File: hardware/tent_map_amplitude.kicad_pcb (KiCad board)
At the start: 4 copper layers, 58 x 61.8 mm, 57 parts, among them U1 LM339AN, U2 TL082IP, U3 TL082IP, U4 LF398_DIP8, U5 LF398_DIP8, U6 LF398_DIP8

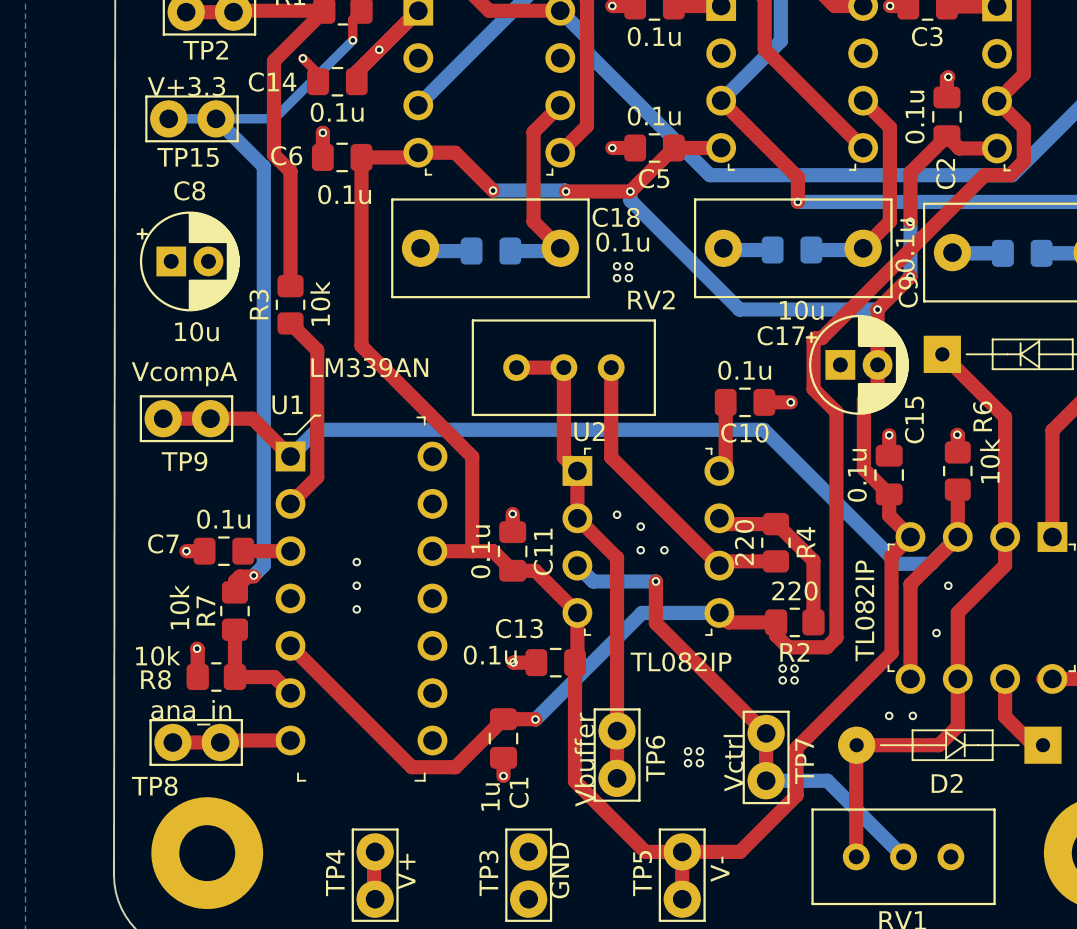
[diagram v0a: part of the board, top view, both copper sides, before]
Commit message: Use extra comparator for sampled bitstream output
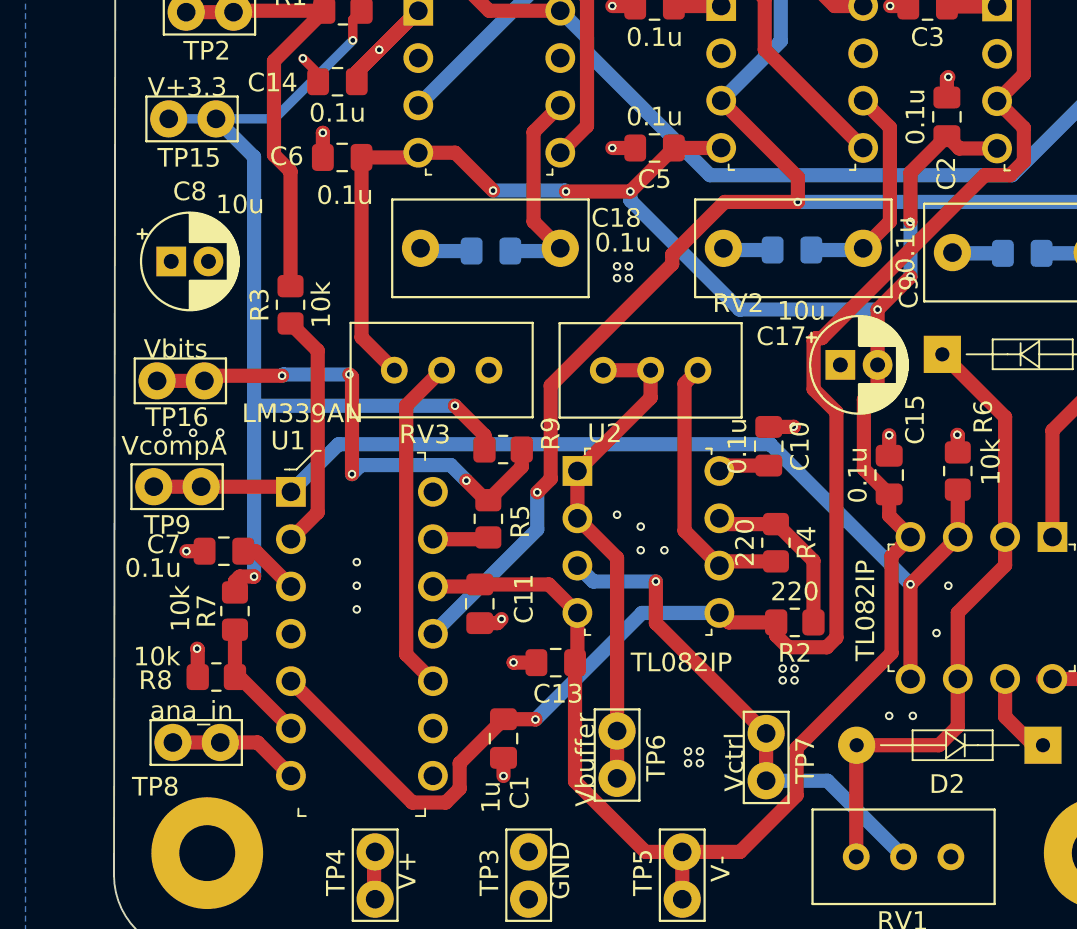
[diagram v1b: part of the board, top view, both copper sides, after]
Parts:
- added G***: LOGO, art:squad, B.Cu at (89.2, 102.3)
- added G***: LOGO, art:sawtooth, B.Cu at (76.3, 72.1)
- added R5: 10k, Resistor_SMD:R_0805_2012Metric_Pad1.20x1.40mm_HandSolder, F.Cu at (85.8, 91.0)
- added R9: 10k, Resistor_SMD:R_0805_2012Metric_Pad1.20x1.40mm_HandSolder, F.Cu at (86.6, 87.3)
- added RV3: R_POT, Potentiometer_THT:Potentiometer_Bourns_3296W_Vertical, F.Cu at (80.8, 83.0)
- added TP16: Vbits, TestPoint:TestPoint_Bridge_Pitch2.54mm_Drill1.0mm, F.Cu at (68.0, 83.6)
- moved RV2 4.66 mm to (97.1, 83.1)
- moved TP9 3.68 mm to (67.8, 89.3)
- moved C11 3.32 mm to (85.3, 95.6), turned to 90 degrees
- moved C10 2.68 mm to (100.9, 87.1), turned to 270 degrees
- moved U1 1.89 mm to (75.2, 89.6)
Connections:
- U1 pad 10: GND -> Net-(RV3-Pad2)
- U1 pad 11: V+ -> Net-(TP11-Pad1)
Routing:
- net Net-(TP11-Pad1): track 43.0 -> 76.6 mm, vias 1 -> 2
- net Net-(R5-Pad2): track 0.00 -> 27.6 mm, vias 0 -> 4
- net Net-(RV3-Pad2): track 0.00 -> 18.1 mm
- net V-: track 140.3 -> 128.1 mm
- net +3V3: track 42.3 -> 54.4 mm, vias 2 -> 3
- net Net-(R5-Pad1): track 0.00 -> 3.01 mm
- net Net-(R6-Pad2): track 58.9 -> 56.1 mm, vias 0 -> 1
- net Net-(R3-Pad1): track 10.9 -> 12.8 mm
- net Net-(C1-Pad1): track 87.4 -> 89.0 mm
- net Net-(R4-Pad2): track 16.2 -> 14.7 mm
- net Net-(RV2-Pad2): track 25.8 -> 27.0 mm
- net Net-(R7-Pad2): track 5.88 -> 6.69 mm
- net Net-(TP8-Pad1): track 6.36 -> 7.08 mm
- net GND: track 25.5 -> 25.7 mm, vias 53 -> 56
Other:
- board text added: "Chaotic Crew UAH Senior Design 2020 Tent Map CRNG"
- board text removed: "Chaotic Crew senior design 2020 tent map CRNG"

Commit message: Update PCB with previous commit changes
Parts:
- moved R3 14.8 mm to (74.0, 64.7)
- moved TP2 1.07 mm to (68.5, 63.7)
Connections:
- R3 pad 1: Net-(R3-Pad1) -> Net-(R1-Pad2)
- R3 pad 2: Net-(R1-Pad2) -> Net-(R3-Pad2)
- R9 pad 2: Net-(R5-Pad2) -> Net-(R5-Pad1)
- TP2 pad 1: Net-(R1-Pad2) -> Net-(R3-Pad2)
- U1 pad 2: Net-(R3-Pad1) -> Net-(R1-Pad2)
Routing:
- net Net-(R3-Pad1): track 12.8 -> 0.00 mm
- net Net-(R1-Pad2): track 23.7 -> 31.9 mm
- net Net-(R5-Pad1): track 3.01 -> 8.88 mm
- net Net-(R3-Pad2): track 0.00 -> 5.49 mm
- net Net-(R5-Pad2): track 27.6 -> 24.2 mm

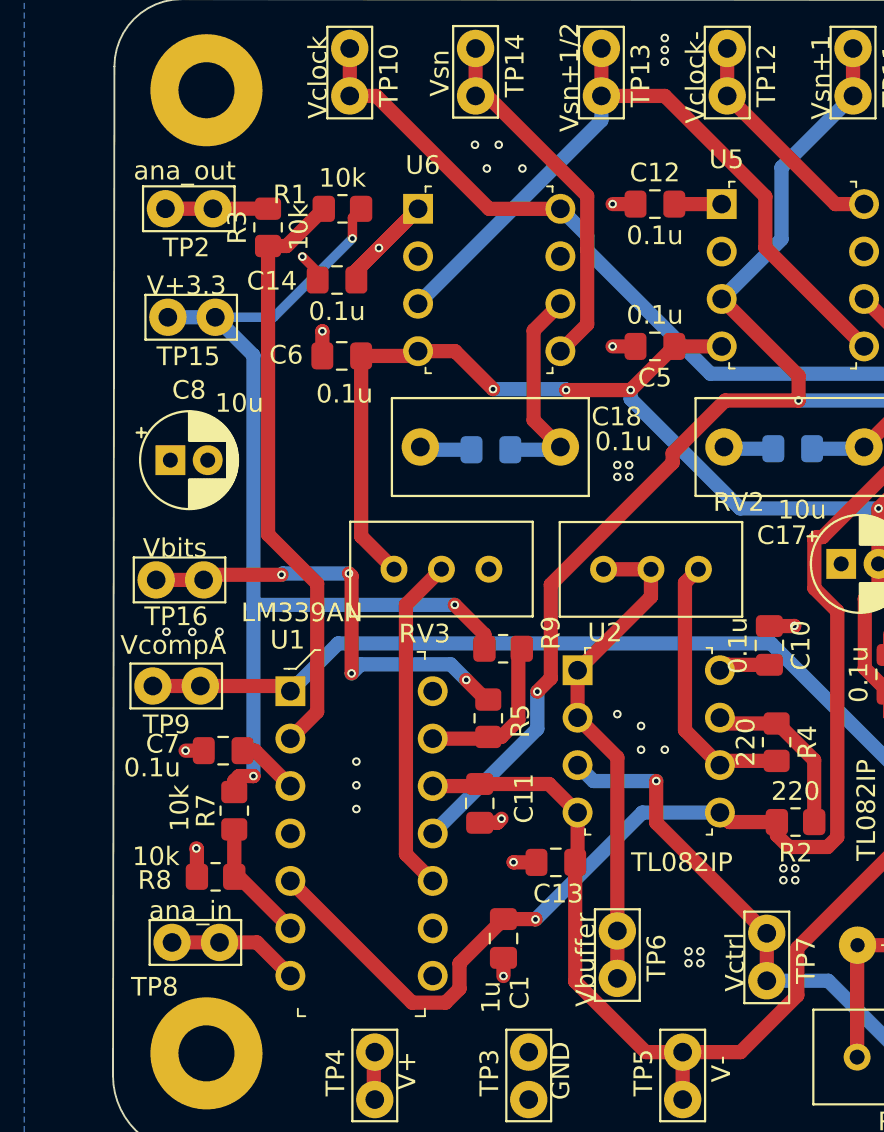
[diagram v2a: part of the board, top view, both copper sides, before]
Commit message: Change resistors back, change resistors to properly do 0v to 3.3v output, add power switch jumper, change references to 3.3v to Va+
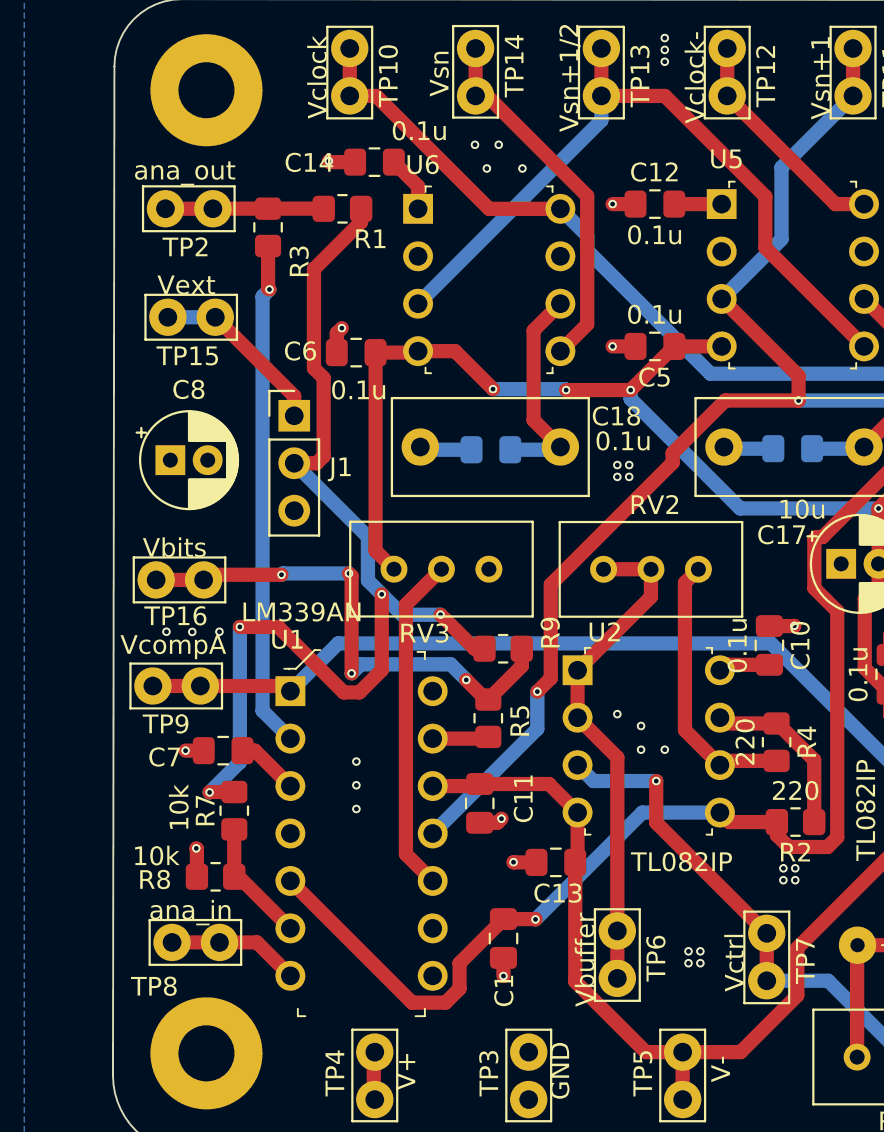
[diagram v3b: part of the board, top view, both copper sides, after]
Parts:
- added J1: Conn_01x03_Male, Connector_PinHeader_2.54mm:PinHeader_1x03_P2.54mm_Vertical, F.Cu at (75.4, 74.8)
- R1, R9: value 10k -> 6.65k
- TP15: value V+3.3 -> Vext
- moved C14 6.62 mm to (79.7, 61.3)
- moved C6 0.79 mm to (78.7, 71.5)
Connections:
- R1 pad 1: +3V3 -> Va+
- R3 pad 1: Net-(R1-Pad2) -> Net-(R3-Pad1)
- R3 pad 2: Net-(R3-Pad2) -> Net-(R1-Pad2)
- R7 pad 1: +3V3 -> Va+
- R9 pad 1: +3V3 -> Va+
- R9 pad 2: Net-(R5-Pad1) -> Net-(R5-Pad2)
- TP15 pad 1: +3V3 -> Net-(J1-Pad1)
- TP2 pad 1: Net-(R3-Pad2) -> Net-(R1-Pad2)
- U1 pad 14: Net-(U1-Pad14) -> (no net)
- U1 pad 2: Net-(R1-Pad2) -> Net-(R3-Pad1)
- U4 pad 2: Net-(U4-Pad2) -> (no net)
- U5 pad 2: Net-(U5-Pad2) -> (no net)
- U6 pad 2: Net-(U6-Pad2) -> (no net)
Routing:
- net Va+: track 0.00 -> 56.4 mm, vias 0 -> 4
- net +3V3: track 54.4 -> 0.00 mm, vias 3 -> 0
- net Net-(R3-Pad1): track 0.00 -> 27.2 mm, vias 0 -> 1
- net Net-(R1-Pad2): track 31.9 -> 8.48 mm
- net Net-(J1-Pad1): track 0.00 -> 12.1 mm
- net V+: track 29.2 -> 22.4 mm, vias 2 -> 1
- net Net-(R5-Pad1): track 8.88 -> 3.01 mm
- net Net-(R3-Pad2): track 5.49 -> 0.00 mm
- net Net-(R5-Pad2): track 24.2 -> 27.6 mm
- net V-: track 128.1 -> 127.1 mm

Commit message: Export gerbers gerbers for pcb V4
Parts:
- moved C8 51.6 mm to (119.2, 88.2)
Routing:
- net GND: vias 56 -> 48
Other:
- board text added: "V+"
- board text added: "Va+ select"
- board text added: "Vext"
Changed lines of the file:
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@@
   (general
     (thickness 1.6002)
-    (drawings 10)
-    (tracks 361)
+    (drawings 27)
+    (tracks 353)
     (zones 0)
     (modules 64)
@@
     (2 In2.Cu power)
     (31 Back signal)
-    (36 B.SilkS user hide)
+    (36 B.SilkS user)
     (37 F.SilkS user)
     (38 B.Mask user)
@@
     (45 Margin user)
     (46 B.CrtYd user)
-    (47 F.CrtYd user)
+    (47 F.CrtYd user hide)
     (49 F.Fab user hide)
   )
@@
       (effects (font (size 0.5 0.5) (thickness 0.08)))
     )
-    (pad 2 smd roundrect (at 1 0) (size 1.2 1.4) (layers Front F.Paste F.Mask) (roundrect_rratio 0.208333)
+    (pad 2 smd roundrect (at 1 0) (size 1.2 1.4) (layers Front F.Paste F.Mask) (roundrect_rratio 0.2083325)
       (net 25 "Net-(R5-Pad2)"))
-    (pad 1 smd roundrect (at -1 0) (size 1.2 1.4) (layers Front F.Paste F.Mask) (roundrect_rratio 0.208333)
+    (pad 1 smd roundrect (at -1 0) (size 1.2 1.4) (layers Front F.Paste F.Mask) (roundrect_rratio 0.2083325)
       (net 28 Va+))
     (model ${KISYS3DMOD}/Resistor_SMD.3dshapes/R_0805_2012Metric.wrl
@@
       (effects (font (size 0.5 0.5) (thickness 0.08)))
     )
-    (pad 2 smd roundrect (at 1 0 90) (size 1.2 1.4) (layers Front F.Paste F.Mask) (roundrect_rratio 0.208333)
+    (pad 2 smd roundrect (at 1 0 90) (size 1.2 1.4) (layers Front F.Paste F.Mask) (roundrect_rratio 0.2083325)
       (net 25 "Net-(R5-Pad2)"))
-    (pad 1 smd roundrect (at -1 0 90) (size 1.2 1.4) (layers Front F.Paste F.Mask) (roundrect_rratio 0.208333)
+    (pad 1 smd roundrect (at -1 0 90) (size 1.2 1.4) (layers Front F.Paste F.Mask) (roundrect_rratio 0.2083325)
       (net 26 "Net-(R5-Pad1)"))
     (model ${KISYS3DMOD}/Resistor_SMD.3dshapes/R_0805_2012Metric.wrl
@@
   )
   (module Capacitor_THT:CP_Radial_D5.0mm_P2.00mm (layer Front)
-    (at 68.78066 77.20838)
+    (at 119.21744 88.18372)
     (descr "CP, Radial series, Radial, pin pitch=2.00mm, , diameter=5mm, Electrolytic Capacitor")
     (tags "CP Radial series Radial pin pitch 2.00mm  diameter 5mm Electrolytic Capacitor")
-    (fp_text reference C8 (at 1 -3.75) (layer F.SilkS)
+    (fp_text reference C8 (at -1.5494 -3.0226) (layer F.SilkS)
       (effects (font (size 1 1) (thickness 0.15)))
     )
@@
   (module digikey-footprints:Diode_DO-35_P10mm (layer Front)
     (at 110.1674 82.1944)
-    (fp_text reference D1 (at 9.7536 2.6416) (layer F.SilkS)
+    (fp_text reference D1 (at 8.93828 -1.94056) (layer F.SilkS)
       (effects (font (size 1 1) (thickness 0.15)))
     )
@@
     )
   )
+  (gr_text "Va+ select" (at 69.54012 77.11948) (layer F.SilkS)
+    (effects (font (size 0.762 0.762) (thickness 0.127)))
+  )
+  (gr_line (start 72.88784 81.026) (end 73.69556 81.026) (layer F.SilkS) (width 0.127))
+  (gr_line (start 72.88784 77.70368) (end 72.88784 81.026) (layer F.SilkS) (width 0.127))
+  (gr_line (start 73.77176 77.70368) (end 72.88784 77.70368) (layer F.SilkS) (width 0.127))
+  (gr_line (start 72.51192 79.15656) (end 72.19696 79.44612) (layer F.SilkS) (width 0.127))
+  (gr_line (start 72.50176 79.10576) (end 72.25792 78.78572) (layer F.SilkS) (width 0.127))
+  (gr_line (start 71.3994 79.04988) (end 72.50176 79.10576) (layer F.SilkS) (width 0.127))
+  (gr_line (start 72.88276 77.37348) (end 73.74128 77.37348) (layer F.SilkS) (width 0.127))
+  (gr_line (start 72.88276 74.03592) (end 72.88276 77.37348) (layer F.SilkS) (width 0.127))
+  (gr_line (start 73.8124 74.03592) (end 72.88276 74.03592) (layer F.SilkS) (width 0.127))
+  (gr_line (start 72.75576 75.184) (end 72.37476 75.54468) (layer F.SilkS) (width 0.127))
+  (gr_line (start 72.75576 75.16368) (end 72.38492 74.86396) (layer F.SilkS) (width 0.127))
+  (gr_line (start 71.47052 75.1332) (end 72.75576 75.16368) (layer F.SilkS) (width 0.127))
+  (gr_line (start 71.6534 75.15352) (end 73.70064 75.09764) (layer Cmts.User) (width 0.15))
+  (gr_line (start 71.72452 75.08748) (end 73.8378 75.14336) (layer Cmts.User) (width 0.15))
+  (gr_text V+ (at 70.13448 79.07528) (layer F.SilkS)
+    (effects (font (size 1 1) (thickness 0.125) italic))
+  )
+  (gr_text Vext (at 69.6468 75.1078) (layer F.SilkS)
+    (effects (font (size 1 1) (thickness 0.15) italic))
+  )
   (gr_arc (start 120.141638 56.134) (end 123.698 56.134) (angle -90) (layer Edge.Cuts) (width 0.001))
   (gr_arc (start 69.3928 56.134) (end 69.3928 52.5272) (angle -90) (layer Edge.Cuts) (width 0.1))
@@
   (segment (start 110.4138 67.3862) (end 110.49 67.31) (width 0.762) (layer Front) (net 1))
   (segment (start 110.4138 68.41) (end 110.4138 67.3862) (width 0.762) (layer Front) (net 1) (status 10))
-  (via (at 96.52 103.505) (size 0.4572) (drill 0.254) (layers Front Back) (net 1))
-  (via (at 96.52 104.14) (size 0.4572) (drill 0.254) (layers Front Back) (net 1))
-  (via (at 97.155 104.14) (size 0.4572) (drill 0.254) (layers Front Back) (net 1))
-  (via (at 97.155 103.505) (size 0.4572) (drill 0.254) (layers Front Back) (net 1))
-  (via (at 101.6 99.06) (size 0.4572) (drill 0.254) (layers Front Back) (net 1))
-  (via (at 102.235 99.06) (size 0.4572) (drill 0.254) (layers Front Back) (net 1))
-  (via (at 102.235 99.695) (size 0.4572) (drill 0.254) (layers Front Back) (net 1))
-  (via (at 101.6 99.695) (size 0.4572) (drill 0.254) (layers Front Back) (net 1))
   (via (at 92.71 77.47) (size 0.4572) (drill 0.254) (layers Front Back) (net 1))
   (via (at 93.345 77.47) (size 0.4572) (drill 0.254) (layers Front Back) (net 1))
@@
   (via (at 108.585 101.6) (size 0.4572) (drill 0.254) (layers Front Back) (net 1))
   (via (at 120.015 92.075) (size 0.4572) (drill 0.254) (layers Front Back) (net 1))
-  (via (at 120.015 90.805) (size 0.4572) (drill 0.254) (layers Front Back) (net 1))
-  (via (at 120.015 89.535) (size 0.4572) (drill 0.254) (layers Front Back) (net 1))
-  (via (at 120.015 88.265) (size 0.4572) (drill 0.254) (layers Front Back) (net 1))
-  (via (at 78.74 95.885) (size 0.4572) (drill 0.254) (layers Front Back) (net 1))
-  (via (at 78.74 94.615) (size 0.4572) (drill 0.254) (layers Front Back) (net 1))
-  (via (at 78.74 93.345) (size 0.4572) (drill 0.254) (layers Front Back) (net 1))
-  (via (at 93.98 91.44) (size 0.4572) (drill 0.254) (layers Front Back) (net 1))
-  (via (at 93.98 92.71) (size 0.4572) (drill 0.254) (layers Front Back) (net 1))
-  (via (at 95.25 92.71) (size 0.4572) (drill 0.254) (layers Front Back) (net 1))
-  (via (at 92.71 90.805) (size 0.4572) (drill 0.254) (layers Front Back) (net 1))
   (via (at 114.935 54.61) (size 0.4572) (drill 0.254) (layers Front Back) (net 1))
   (via (at 102.18674 86.07806) (size 0.4572) (drill 0.254) (layers Front Back) (net 1))
@@
   (segment (start 77.69116 70.41116) (end 77.96276 70.13956) (width 0.762) (layer Front) (net 1))
   (segment (start 77.69116 71.4502) (end 77.69116 70.41116) (width 0.762) (layer Front) (net 1))
+  (via (at 121.60504 92.06992) (size 0.4572) (drill 0.254) (layers Front Back) (net 1))
+  (via (at 119.11076 93.64472) (size 0.4572) (drill 0.254) (layers Front Back) (net 1))
+  (via (at 119.95912 94.42704) (size 0.4572) (drill 0.254) (layers Front Back) (net 1))
+  (via (at 120.71604 94.48292) (size 0.4572) (drill 0.254) (layers Front Back) (net 1))
+  (via (at 121.60504 94.4626) (size 0.4572) (drill 0.254) (layers Front Back) (net 1))
+  (via (at 122.41276 93.86316) (size 0.4572) (drill 0.254) (layers Front Back) (net 1))
+  (via (at 96.266 101.346) (size 0.4572) (drill 0.254) (layers Front Back) (net 1))
+  (via (at 97.028 101.346) (size 0.4572) (drill 0.254) (layers Front Back) (net 1))
+  (via (at 97.028 102.108) (size 0.4572) (drill 0.254) (layers Front Back) (net 1))
+  (via (at 96.266 102.108) (size 0.4572) (drill 0.254) (layers Front Back) (net 1))
   (segment (start 98.70948 96.5835) (end 98.20148 96.0755) (width 0.762) (layer Front) (net 2) (status 30))
   (segment (start 101.24948 96.5835) (end 98.70948 96.5835) (width 0.762) (layer Front) (net 2) (status 30))
